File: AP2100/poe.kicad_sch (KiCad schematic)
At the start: 133 parts, among them IC2 PM8805TR, IC3 PM8804TR, J1 0826-1X1T-GH-F, J2 Barrel_Jack, Q1 BSC190N15NS3GATMA1, Q2 PBSS4240T, Q3 PBSS4240T, Q4 FDMC86259P, Q5 FOD817AS, U4 STL90N6F7, U5 STL90N6F7, U6 TS2431-AILT

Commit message: More cleanups
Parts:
- J2: PartsBoxID (none) -> BJ-2.5MM
- renumbered D14 to D10, D15 to D11, D16 to D12, D18 to D13, D19 to D14, D20 to D15, D21 to D16, D22 to D17, D23 to D18, D24 to D19, D25 to D20, D11 to D7, D12 to D8, D13 to D9, D7 to LED1, D8 to LED2, D9 to LED3, D10 to LED4, D17 to LED5
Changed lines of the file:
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@@
   (junction (at 370.205 144.78) (diameter 0.9144) (color 0 0 0 0))
   (junction (at 370.205 183.515) (diameter 0.9144) (color 0 0 0 0))
-  (no_connect (at 80.645 153.035))
   (no_connect (at 85.725 153.035))
+  (no_connect (at 80.645 153.035))
   (no_connect (at 90.805 191.135))
   (wire (pts (xy 48.26 45.085) (xy 52.07 45.085))
@@
   (symbol (lib_id "Device:D_Schottky_ALT") (at 113.03 111.76 270) (unit 1)
     (in_bom yes) (on_board yes)
-    (property "Reference" "D13" (id 0) (at 114.935 109.22 90)
+    (property "Reference" "D9" (id 0) (at 114.935 109.22 90)
       (effects (font (size 1.27 1.27)) (justify left))
     )
@@
   (symbol (lib_id "Device:D_ALT") (at 127.635 164.465 0) (unit 1)
     (in_bom yes) (on_board yes)
-    (property "Reference" "D18" (id 0) (at 127.635 160.02 0))
+    (property "Reference" "D13" (id 0) (at 127.635 160.02 0))
     (property "Value" "BAS16J" (id 1) (at 127.635 161.925 0))
     (property "Footprint" "Diode_SMD:D_SOD-323" (id 2) (at 127.635 164.465 0)
@@
   (symbol (lib_id "Device:D_ALT") (at 132.08 193.675 270) (unit 1)
     (in_bom yes) (on_board yes)
-    (property "Reference" "D23" (id 0) (at 127.635 193.04 90))
+    (property "Reference" "D18" (id 0) (at 127.635 193.04 90))
     (property "Value" "BAS70" (id 1) (at 127 195.58 90))
     (property "Footprint" "Diode_SMD:D_SOD-323" (id 2) (at 132.08 193.675 0)
@@
   (symbol (lib_id "Device:D_ALT") (at 142.24 144.145 270) (unit 1)
     (in_bom yes) (on_board yes)
-    (property "Reference" "D16" (id 0) (at 144.78 142.24 90)
+    (property "Reference" "D12" (id 0) (at 144.78 142.24 90)
       (effects (font (size 1.27 1.27)) (justify left))
     )
@@
   (symbol (lib_id "Device:D_ALT") (at 147.955 138.43 0) (unit 1)
     (in_bom yes) (on_board yes)
-    (property "Reference" "D15" (id 0) (at 148.59 132.08 0))
+    (property "Reference" "D11" (id 0) (at 148.59 132.08 0))
     (property "Value" "BAS16J" (id 1) (at 148.59 134.62 0))
     (property "Footprint" "Diode_SMD:D_SOD-323" (id 2) (at 147.955 138.43 0)
@@
   (symbol (lib_id "Device:D_ALT") (at 193.675 167.64 270) (unit 1)
     (in_bom yes) (on_board yes)
-    (property "Reference" "D20" (id 0) (at 194.437 165.354 90)
+    (property "Reference" "D15" (id 0) (at 194.437 165.354 90)
       (effects (font (size 1.27 1.27)) (justify left))
     )
@@
   (symbol (lib_id "Device:D_Zener_ALT") (at 206.375 174.625 270) (unit 1)
     (in_bom yes) (on_board yes)
-    (property "Reference" "D22" (id 0) (at 207.645 175.26 90)
+    (property "Reference" "D17" (id 0) (at 207.645 175.26 90)
       (effects (font (size 1.27 1.27)) (justify left))
     )
@@
   (symbol (lib_id "Device:D_ALT") (at 212.725 203.2 270) (unit 1)
     (in_bom yes) (on_board yes)
-    (property "Reference" "D24" (id 0) (at 210.82 200.66 90))
+    (property "Reference" "D19" (id 0) (at 210.82 200.66 90))
     (property "Value" "BAS70" (id 1) (at 212.09 205.74 90))
     (property "Footprint" "Diode_SMD:D_SOD-323" (id 2) (at 212.725 203.2 0)
@@
   (symbol (lib_id "Device:D_ALT") (at 223.52 210.185 0) (unit 1)
     (in_bom yes) (on_board yes)
-    (property "Reference" "D25" (id 0) (at 224.155 207.645 0))
+    (property "Reference" "D20" (id 0) (at 224.155 207.645 0))
     (property "Value" "BAS70" (id 1) (at 223.52 212.725 0))
     (property "Footprint" "Diode_SMD:D_SOD-323" (id 2) (at 223.52 210.185 0)
@@
   (symbol (lib_id "Device:D_ALT") (at 247.65 164.465 270) (unit 1)
     (in_bom yes) (on_board yes)
-    (property "Reference" "D19" (id 0) (at 248.412 162.179 90)
+    (property "Reference" "D14" (id 0) (at 248.412 162.179 90)
       (effects (font (size 1.27 1.27)) (justify left))
     )
@@
   (symbol (lib_id "Device:D_Zener_ALT") (at 260.35 171.45 270) (unit 1)
     (in_bom yes) (on_board yes)
-    (property "Reference" "D21" (id 0) (at 261.62 172.085 90)
+    (property "Reference" "D16" (id 0) (at 261.62 172.085 90)
       (effects (font (size 1.27 1.27)) (justify left))
     )
@@
   (symbol (lib_id "Device:D_TVS_ALT") (at 279.4 128.905 270) (unit 1)
     (in_bom yes) (on_board yes)
-    (property "Reference" "D14" (id 0) (at 281.432 127.7366 90)
+    (property "Reference" "D10" (id 0) (at 281.432 127.7366 90)
       (effects (font (size 1.27 1.27)) (justify left))
     )
@@
   (symbol (lib_id "Device:LED_ALT") (at 148.59 86.36 90) (unit 1)
     (in_bom yes) (on_board yes)
-    (property "Reference" "D10" (id 0) (at 145.415 86.36 90))
+    (property "Reference" "LED4" (id 0) (at 144.78 86.36 90))
     (property "Value" "AUX" (id 1) (at 151.765 86.36 90))
     (property "Footprint" "LED_SMD:LED_0603_1608Metric" (id 2) (at 148.59 86.36 0)
@@
   (symbol (lib_id "Device:LED_ALT") (at 170.18 75.565 90) (unit 1)
     (in_bom yes) (on_board yes)
-    (property "Reference" "D7" (id 0) (at 173.1772 74.5744 90)
+    (property "Reference" "LED1" (id 0) (at 173.1772 74.5744 90)
       (effects (font (size 1.27 1.27)) (justify right))
     )
@@
   (symbol (lib_id "Device:LED_ALT") (at 179.07 75.565 90) (unit 1)
     (in_bom yes) (on_board yes)
-    (property "Reference" "D8" (id 0) (at 182.0672 74.5744 90)
+    (property "Reference" "LED2" (id 0) (at 182.0672 74.5744 90)
       (effects (font (size 1.27 1.27)) (justify right))
     )
@@
   (symbol (lib_id "Device:LED_ALT") (at 189.23 75.565 90) (unit 1)
     (in_bom yes) (on_board yes)
-    (property "Reference" "D9" (id 0) (at 192.2272 74.5744 90)
+    (property "Reference" "LED3" (id 0) (at 192.2272 74.5744 90)
       (effects (font (size 1.27 1.27)) (justify right))
     )
@@
   (symbol (lib_id "Device:LED_ALT") (at 370.205 163.83 90) (unit 1)
     (in_bom yes) (on_board yes)
-    (property "Reference" "D17" (id 0) (at 372.11 161.925 90)
+    (property "Reference" "LED5" (id 0) (at 372.11 161.925 90)
       (effects (font (size 1.27 1.27)) (justify right))
     )
@@
   (symbol (lib_id "AP2100-rescue:STPS4S200S-STPS4S200S") (at 135.89 89.535 180) (unit 1)
     (in_bom yes) (on_board yes)
-    (property "Reference" "D11" (id 0) (at 128.27 82.804 0))
+    (property "Reference" "D7" (id 0) (at 128.27 82.804 0))
     (property "Value" "STPS4S200S" (id 1) (at 128.27 85.1154 0))
     (property "Footprint" "LIB_STPS4S200S:DIOM8059X265N" (id 2) (at 124.46 89.535 0)
@@
       (effects (font (size 1.27 1.27)) hide)
     )
+    (property "PartsBoxID" "BJ-2.5MM" (id 4) (at 107.95 92.075 0)
+      (effects (font (size 1.27 1.27)) hide)
+    )
   )
   (symbol (lib_id "Device:Q_NPN_BEC") (at 219.075 168.91 0) (unit 1)
@@
   (symbol (lib_id "Diode:BAV70") (at 290.83 90.17 180) (unit 1)
     (in_bom yes) (on_board yes)
-    (property "Reference" "D12" (id 0) (at 290.83 93.345 0))
+    (property "Reference" "D8" (id 0) (at 290.83 93.345 0))
     (property "Value" "BAV70" (id 1) (at 290.83 95.6564 0))
     (property "Footprint" "Package_TO_SOT_SMD:SOT-23" (id 2) (at 290.83 90.17 0)

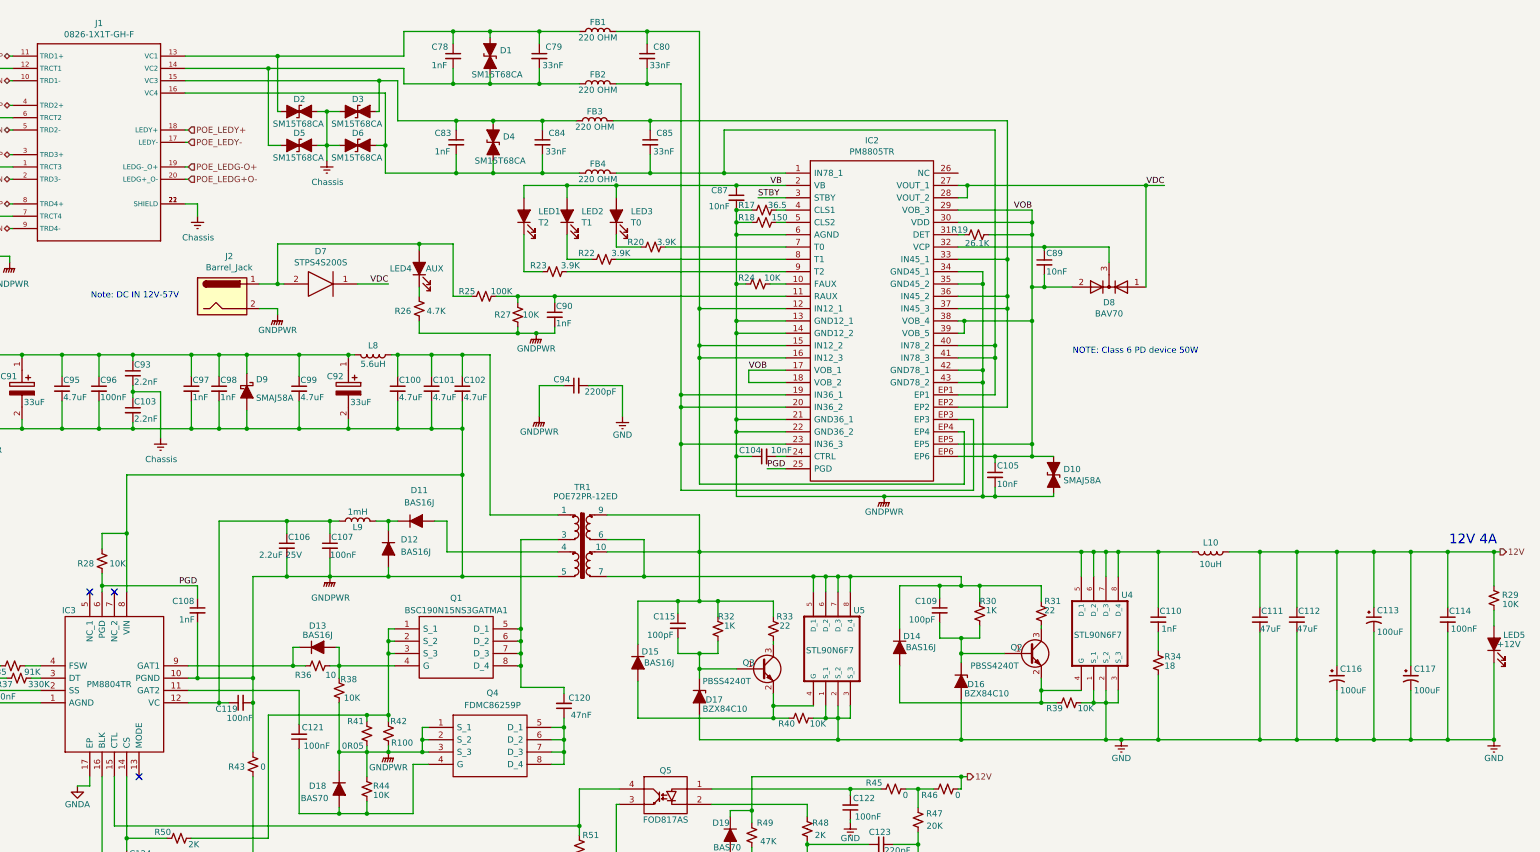
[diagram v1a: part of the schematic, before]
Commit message: Cleanups per ST Micro's review. Add old and old-old kinda by accident
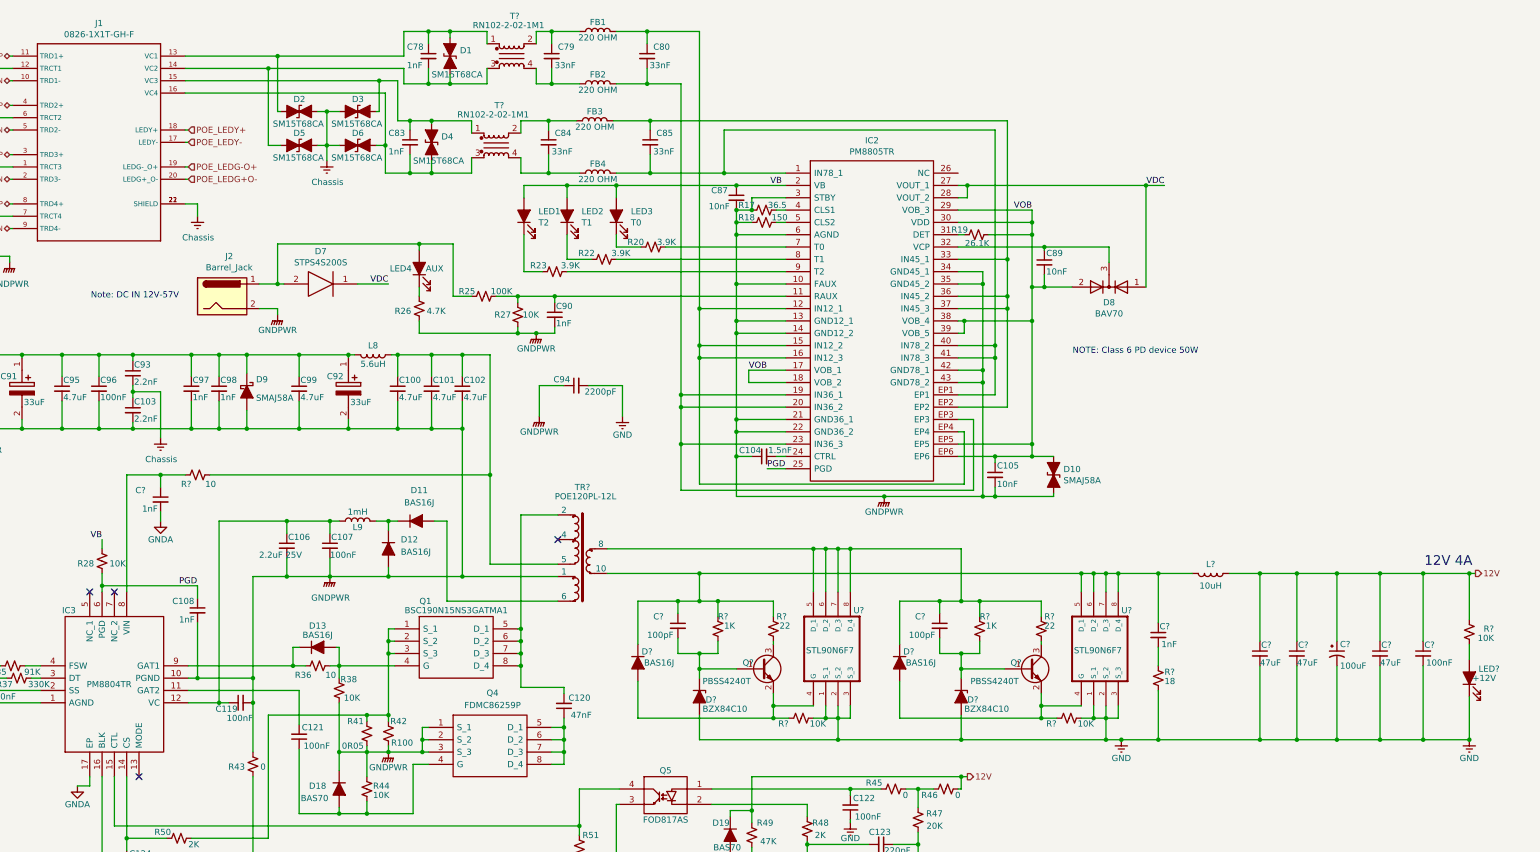
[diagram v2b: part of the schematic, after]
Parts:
- removed C109, C115: 100pF, Capacitor_SMD:C_0805_2012Metric, symbol Device:C_Small
- removed C110: 1nF, Capacitor_SMD:C_0805_2012Metric, symbol Device:C_Small
- removed C111, C112: 47uF, Capacitor_SMD:C_1210_3225Metric, symbol Device:C_Small
- removed C113, C116, C117: 100uF, Capacitor_SMD:CP_Elec_6.3x5.9, symbol Device:CP1_Small
- removed C114: 100nF, Capacitor_SMD:C_0603_1608Metric, symbol Device:C_Small
- removed D14, D15: BAS16J, Diode_SMD:D_SOD-323, symbol Device:D_ALT
- removed D16, D17: BZX84C10, Package_TO_SOT_SMD:SOT-23, symbol Device:D_Zener_ALT
- removed L10: 10uH, LIB_7443631000:WE-HCF_201322, symbol 7443631000:7443631000
- removed LED5: +12V, LED_SMD:LED_0603_1608Metric, symbol Device:LED_ALT
- removed Q2, Q3: PBSS4240T, Package_TO_SOT_SMD:SOT-23, symbol Device:Q_NPN_BEC
- removed R24, R29, R39, R40: 10K, Resistor_SMD:R_0603_1608Metric, symbol Device:R_Small_US
- removed R30, R32: 1K, Resistor_SMD:R_0603_1608Metric, symbol Device:R_Small_US
- removed R31, R33: 22, Resistor_SMD:R_0603_1608Metric, symbol Device:R_Small_US
- removed R34: 18, Resistor_SMD:R_0805_2012Metric, symbol Device:R_Small_US
- removed TR1: POE72PR-12ED, Scott:Transformer_Coilcraft_POE72PR, symbol AP2100-rescue:Transformer_TNK_TSE265-Scott
- removed U4, U5: STL90N6F7, Scott:TRANS_STL60P4LLF6, symbol STL90N6F7:STL90N6F7
- added C?: 100uF, Capacitor_SMD:CP_Elec_6.3x5.9, symbol Device:CP1_Small
- added C? (x2): 1nF, Capacitor_SMD:C_0805_2012Metric, symbol Device:C_Small
- added C? (x3): 47uF, Capacitor_SMD:C_1210_3225Metric, symbol Device:C_Small
- added C?: 100nF, Capacitor_SMD:C_0603_1608Metric, symbol Device:C_Small
- added C? (x2): 100pF, Capacitor_SMD:C_0805_2012Metric, symbol Device:C_Small
- added D? (x2): BZX84C10, Package_TO_SOT_SMD:SOT-23, symbol Device:D_Zener_ALT
- added D? (x2): BAS16J, Diode_SMD:D_SOD-323, symbol Device:D_ALT
- added L?: 10uH, LIB_7443631000:WE-HCF_201322, symbol 7443631000:7443631000
- added LED?: +12V, LED_SMD:LED_0603_1608Metric, symbol Device:LED_ALT
- added Q? (x2): PBSS4240T, Package_TO_SOT_SMD:SOT-23, symbol Device:Q_NPN_BEC
- added R? (x3): 10K, Resistor_SMD:R_0603_1608Metric, symbol Device:R_Small_US
- added R? (x2): 22, Resistor_SMD:R_0603_1608Metric, symbol Device:R_Small_US
- added R?: 10, Resistor_SMD:R_0805_2012Metric, symbol Device:R_Small_US
- added R? (x2): 1K, Resistor_SMD:R_0603_1608Metric, symbol Device:R_Small_US
- added R?: 18, Resistor_SMD:R_0805_2012Metric, symbol Device:R_Small_US
- added T? (x2): RN102-2-02-1M1, Inductor_THT:Choke_Schaffner_RN102-04-14.0x14.0mm, symbol Filter:Choke_Schaffner_RN102-2-02-1M1
- added TR?: POE120PL-12L, Scott:Transformer_Coilcraft_POE120PL, symbol Scott:Transformer_POE120PL-12L
- added U? (x2): STL90N6F7, Scott:TRANS_STL60P4LLF6, symbol STL90N6F7:STL90N6F7
- C104: value 10nF -> 1.5nF; PartsBoxID 0603-10nF-X7R-100V -> 0603-1.5nF-X7R-100V
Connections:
- net STBY is gone; now on net GNDPWR: IC2.3 (STBY)
- net 12V: now also C?.1, C?.1, C?.1, C?.1, C?.1, L?.2, R?.2
- net GND: now also C?.2, C?.2, C?.2, C?.2, C?.2, D?.2 (A), D?.2 (A), LED?.1 (K), R?.1, R?.1, R?.2, U?.1 (S_1), U?.1 (S_1), U?.2 (S_2), U?.2 (S_2), U?.3 (S_3), U?.3 (S_3)
- net GNDA: now also C?.2
- net GNDPWR: now also IC2.10 (FAUX), TR?.1; no longer IC3.8 (VIN), R28.1
- net VB: now also R28.1
- net at C78.1, D1.1 (A1), D2.2 (A2)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: now also T?.1; no longer C79.1, FB1.1
- net at C78.2, D1.2 (A2), D5.2 (A2)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: now also T?.3; no longer C79.2, FB2.1
- net at C83.1, D3.1 (A1), D4.1 (A1)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: now also T?.1; no longer C84.1, FB3.1
- net at C83.2, D4.2 (A2), D6.1 (A1)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: now also T?.3; no longer C84.2, FB4.1
- net at D11.2 (A): now also TR?.6
- net at C120.2, Q1.5 (D_1), Q1.6 (D_2)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: now also TR?.2
- net at C100.1, C101.1, C102.1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: now also R?.2, TR?.5
- new net: C?.1, IC3.8 (VIN), R?.1
- new net: C79.1, FB1.1, T?.2
- new net: C79.2, FB2.1, T?.4
- new net: C84.1, FB3.1, T?.2
- new net: C84.2, FB4.1, T?.4
- new net: C?.2, D?.1 (K), Q?.1 (B), R?.2 (x2)
- new net: LED?.2 (A), R?.1
- new net: C?.1, D?.1 (K), R?.1, R?.1, TR?.8, U?.5 (D_1), U?.6 (D_2), U?.7 (D_3), U?.8 (D_4)
- new net: Q?.3 (C), R?.2 (x2)
- new net: D?.2 (A), Q?.2 (E), R?.2, U?.4 (G) (x2)
- new net: C?.1, C?.1, D?.1 (K), L?.1, R?.1, R?.1, TR?.10, U?.5 (D_1), U?.6 (D_2), U?.7 (D_3), U?.8 (D_4)
- new net: C?.2, R?.1
- no-connect marks 3 -> 4
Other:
- moved on the sheet: C78, C79, C83, C84, D1, D4

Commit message: More PoE layout
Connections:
- net VDC: now also D8.2 (A); no longer D8.1 (A)
- net VOB: now also D8.1 (A); no longer D8.2 (A)
- net IN_78: now reaches C85.2, FB4.2, IC2.1 (IN78_1), IC2.40 (IN78_2), IC2.41 (IN78_3), IC2.EP1
- net IN_12: now reaches C80.1, FB1.2, IC2.12 (IN12_1), IC2.15 (IN12_2), IC2.16 (IN12_3), IC2.EP4
- net IN_36: now reaches C80.2, FB2.2, IC2.19 (IN36_1), IC2.20 (IN36_2), IC2.23 (IN36_3), IC2.EP3
- net IN_45: now reaches C85.1, FB3.2, IC2.33 (IN45_1), IC2.36 (IN45_2), IC2.37 (IN45_3), IC2.EP2
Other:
- moved on the sheet: D8
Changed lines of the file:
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@@
   (junction (at 365.125 149.225) (diameter 0.9144) (color 0 0 0 0))
   (junction (at 365.125 183.515) (diameter 0.9144) (color 0 0 0 0))
-  (no_connect (at 90.805 191.135))
   (no_connect (at 177.165 142.24))
-  (no_connect (at 85.725 153.035))
+  (no_connect (at 90.805 191.135))
   (no_connect (at 80.645 153.035))
+  (no_connect (at 85.725 153.035))
   (wire (pts (xy 48.26 45.085) (xy 52.07 45.085))
     (stroke (width 0) (type solid) (color 0 0 0 0))
@@
     (effects (font (size 1.27 1.27)) (justify right bottom))
   )
+  (label "IN_36" (at 202.565 48.26 180)
+    (effects (font (size 1.27 1.27)) (justify right bottom))
+  )
+  (label "IN_12" (at 206.375 37.465 180)
+    (effects (font (size 1.27 1.27)) (justify right bottom))
+  )
+  (label "IN_45" (at 215.9 55.88 180)
+    (effects (font (size 1.27 1.27)) (justify right bottom))
+  )
+  (label "IN_78" (at 215.9 57.785 180)
+    (effects (font (size 1.27 1.27)) (justify right bottom))
+  )
   (label "VOB" (at 216.535 107.315 0)
     (effects (font (size 1.27 1.27)) (justify left bottom))
@@
     )
   )
-  (symbol (lib_id "Diode:BAV70") (at 290.83 90.17 180) (unit 1)
+  (symbol (lib_id "Diode:BAV70") (at 290.83 90.17 0) (mirror x) (unit 1)
     (in_bom yes) (on_board yes)
     (property "Reference" "D8" (id 0) (at 290.83 93.345 0))
